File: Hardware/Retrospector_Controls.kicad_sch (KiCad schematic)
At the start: 32 parts, among them J1 Conn_01x08_Female, J10 Feedback_CV, J11 Audio_In_R, J12 Audio_Out_R, J13 Audio_Out_L, J14 Filter, J2 Conn_01x08_Female, J3 Conn_01x08_Female, J4 Conn_01x08_Female, J5 Audio_In_L, J6 Delay_CV_L, J7 Mix_CV, J8 Delay_CV_R, J9 Clock, U1 TB62781FNG

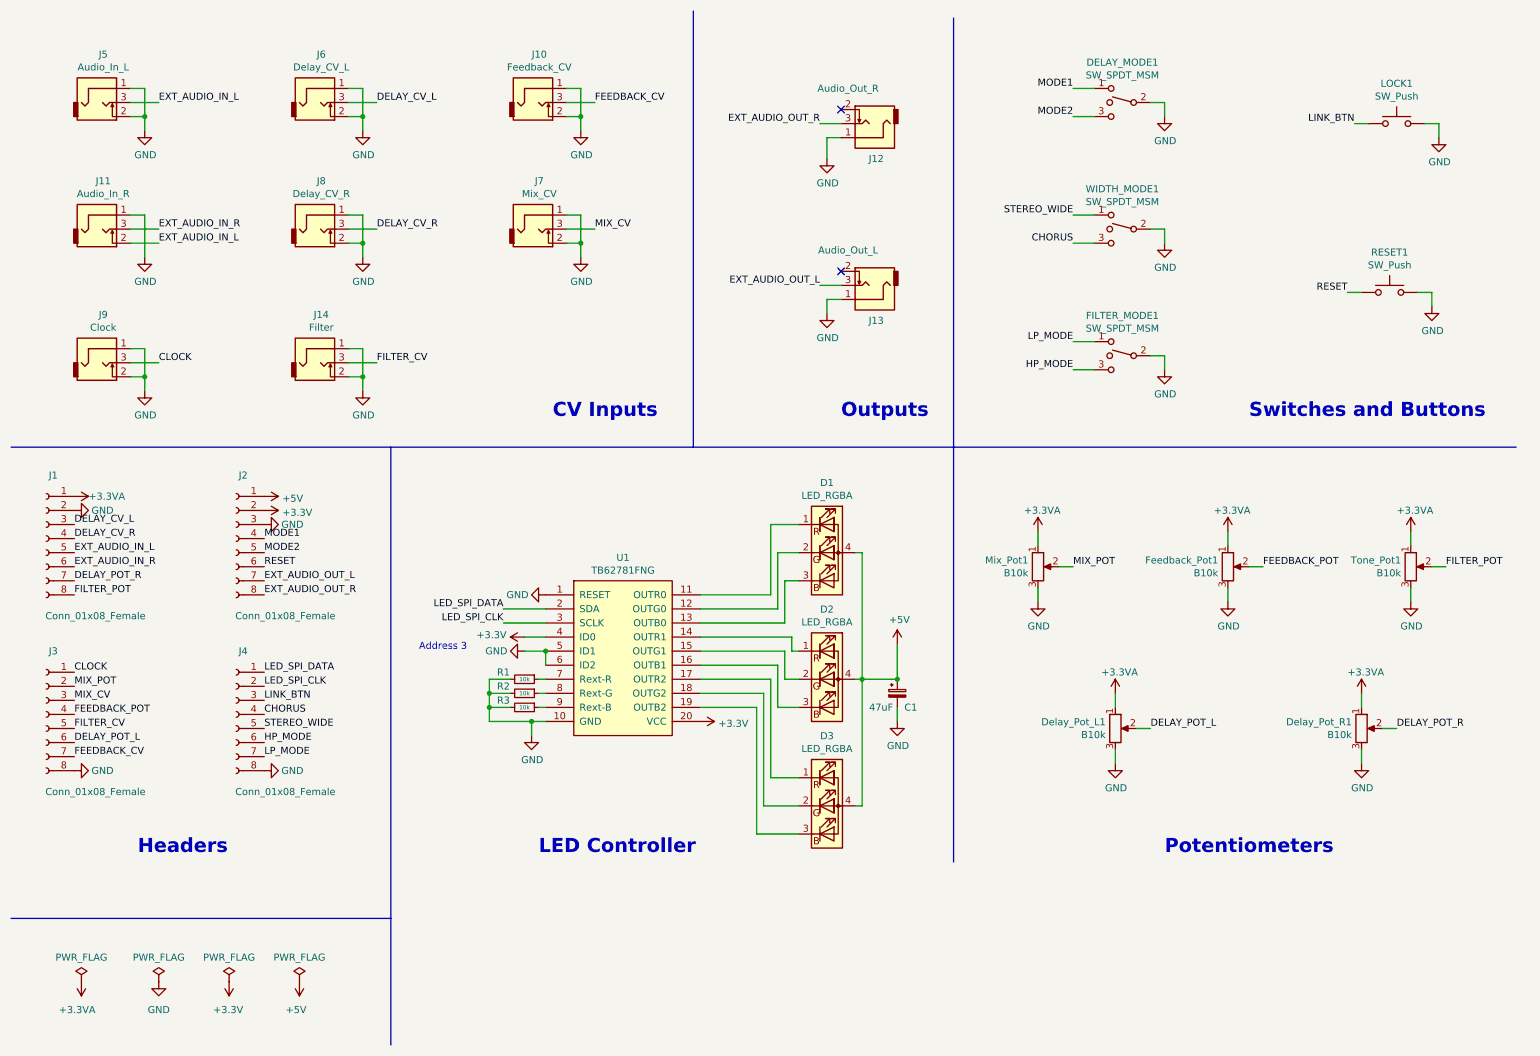
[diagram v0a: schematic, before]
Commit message: Removed old Kicad files
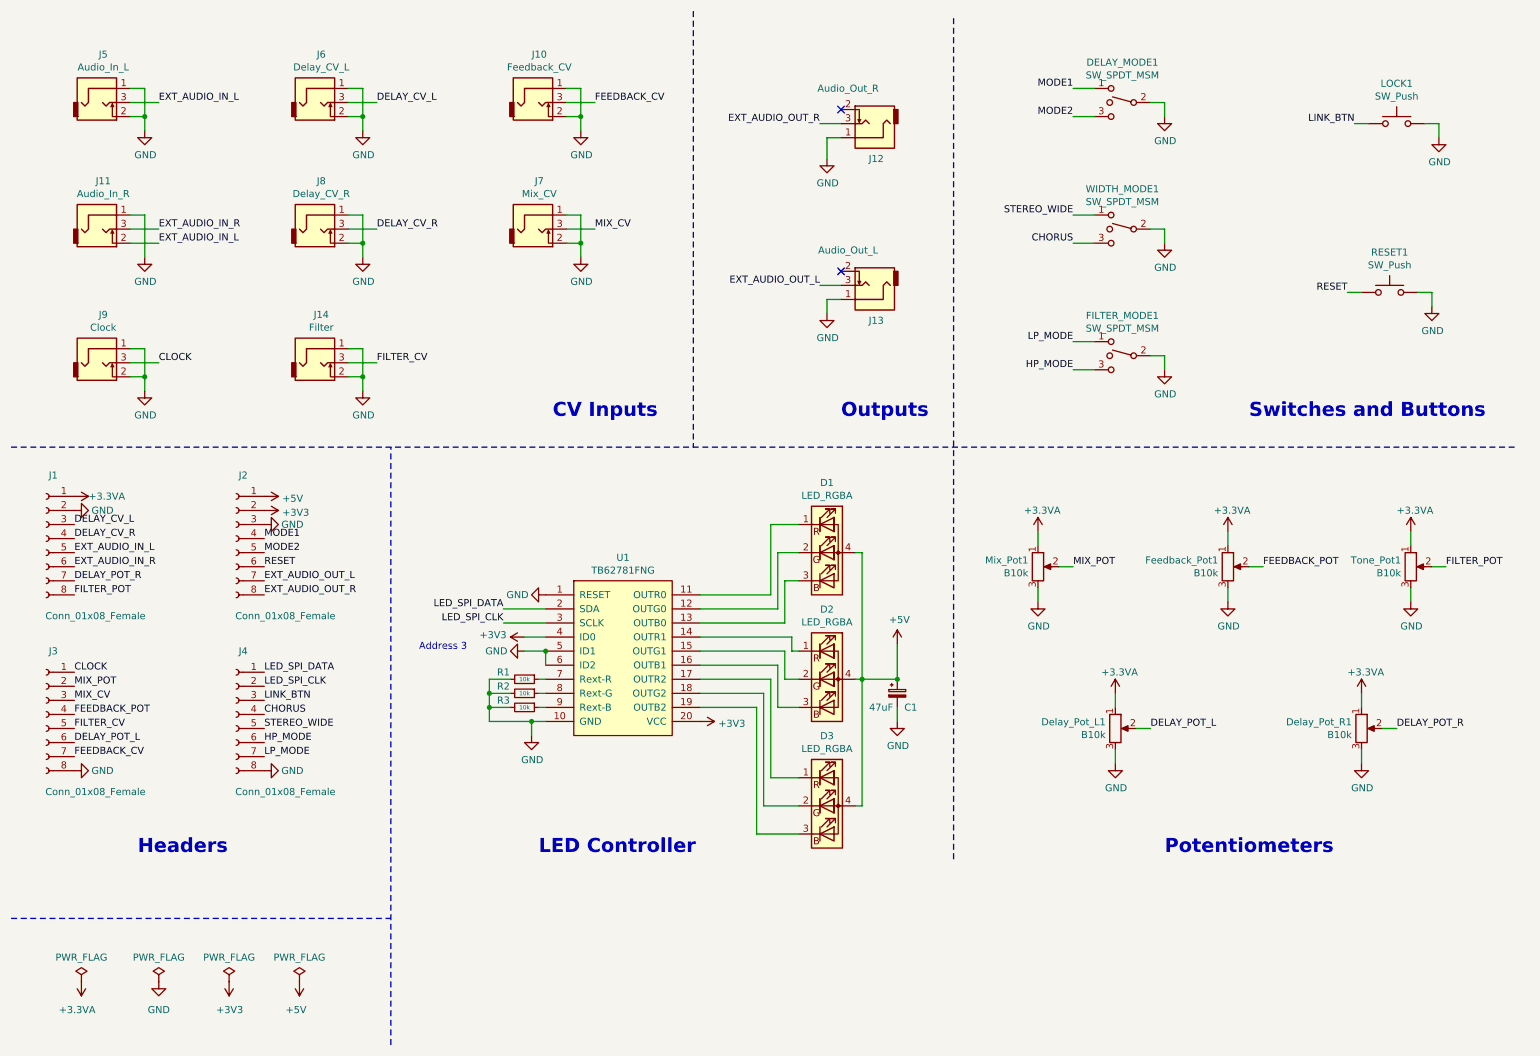
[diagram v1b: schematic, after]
